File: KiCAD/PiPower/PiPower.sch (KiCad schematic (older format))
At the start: 19 parts

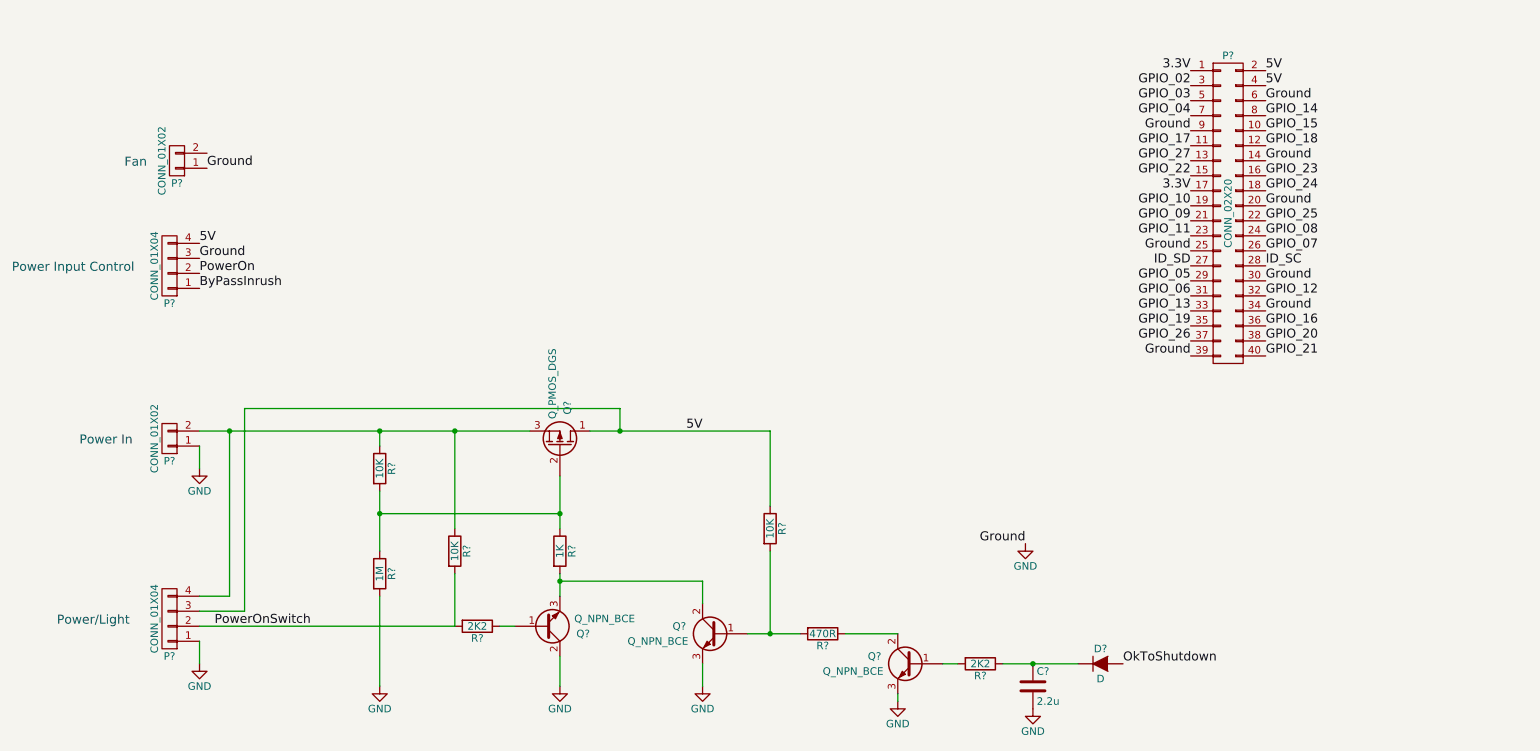
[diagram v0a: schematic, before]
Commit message: Raspberry Pi Power control board
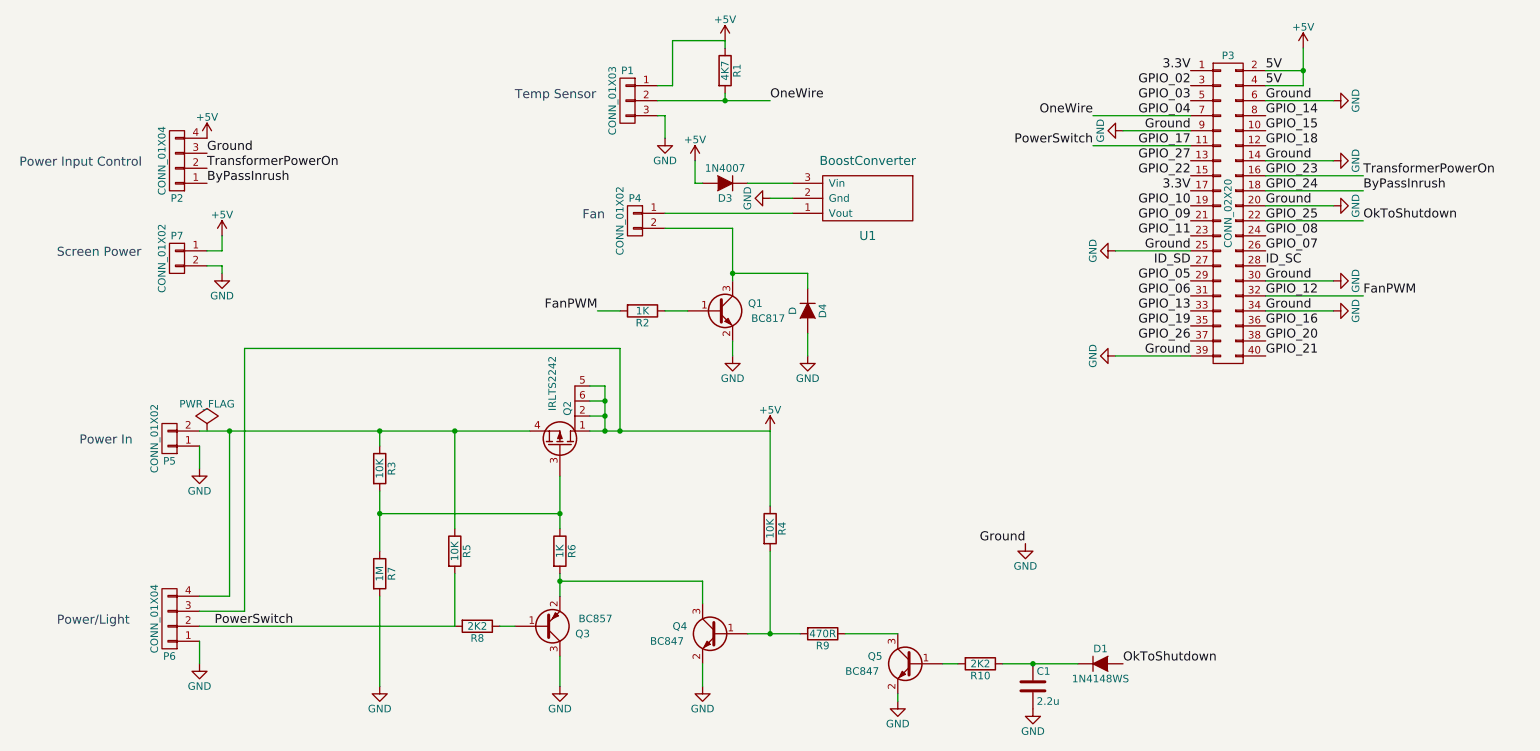
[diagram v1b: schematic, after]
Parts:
- removed P?: CONN_01X02, symbol CONN_01X02
- removed Q?: Q_PMOS_DGS, symbol Q_PMOS_DGS
- removed Q? (x3): Q_NPN_BCE, symbol Q_NPN_BCE
- added D3: 1N4007, Diodes_ThroughHole:Diode_DO-41_SOD81_Horizontal_RM10, symbol D
- added D4: D, Diodes_SMD:SOD-323, symbol D
- added P1: CONN_01X03, PinHead1-4:ThreePinSmall, symbol CONN_01X03
- added P4: CONN_01X02, PinHead1-4:TwoPinSmall, symbol CONN_01X02
- added P7: CONN_01X02, Pin_Headers:Pin_Header_Straight_1x02, symbol CONN_01X02
- added Q1: BC817, TO_SOT_Packages_SMD:SOT-23, symbol Q_NPN_BEC
- added Q2: IRLTS2242, symbol IRLTS2242
- added Q3: BC857, TO_SOT_Packages_SMD:SOT-23, symbol Q_PNP_BEC
- added Q4, Q5: BC847, TO_SOT_Packages_SMD:SOT-23, symbol Q_NPN_BEC
- added R1: 4K7, Resistors_SMD:R_0805, symbol R
- added R2: 1K, Resistors_SMD:R_0805, symbol R
- added U1: BoostConverter, BoostConverter:BoostConverter, symbol BoostConverter
- C1: renamed from C?; footprint (none) -> Capacitors_SMD:C_0805
- D1: renamed from D?; value D -> 1N4148WS; footprint (none) -> Diodes_SMD:SOD-323
- P2, P6: renamed from P?; footprint (none) -> PinHead1-4:PINHeader1-4
- P3: renamed from P?; footprint (none) -> Pin_Headers:Pin_Header_Straight_2x20
- P5: renamed from P?; footprint (none) -> wcon:WCON-2PIN
- R10, R3, R4, R5, R6, R7, R8, R9: renamed from R?; footprint (none) -> Resistors_SMD:R_0805
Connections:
- net GPIO_24 is gone; now on net ByPassInrush: P3.18 (P18)
- net OkToShutdown is gone; now on net GPIO_25: D1.2 (A)
- net PowerOn is gone; now on net GPIO_23: P2.2 (P2)
- net PowerOnSwitch is gone; now on net GPIO_17: P6.2 (P2), R5.2, R8.2
- net GND: now also D4.2 (A), P1.3 (P3), P7.2 (P2), Q1.2 (E), Q3.3 (C), Q4.2 (E), Q5.2 (E), U1.2 (Gnd)
- net GPIO_04: now also P1.2 (P2), R1.2
- net at R3.2, R6.1, R7.1: now also Q2.3 (G)
- net at P5.2 (P2), P6.4 (P4), R3.1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: now also Q2.4 (S)
- net at R6.2: now also Q3.2 (E), Q4.3 (C)
- net at R8.1: now also Q3.1 (B)
- net at R4.2, R9.2: now also Q4.1 (B)
- net at R10.2: now also Q5.1 (B)
- net at R9.1: now also Q5.3 (C)
- net 5V renamed +5V
- net +5V: now also D3.2 (A), P1.1 (P1), P7.1 (P1), Q2.1 (D), Q2.2 (D), Q2.5 (D), Q2.6 (D), R1.1
- net GPIO_12 renamed FanPWM
- net FanPWM: now also R2.2
- new net: Q1.1 (B), R2.1
- new net: D4.1 (K), P4.2 (P2), Q1.3 (C)
- new net: P4.1 (P1), U1.1 (Vout)
- new net: D3.1 (K), U1.3 (Vin)
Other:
- note added: "Fan"
- note added: "Screen Power"
- note added: "Temp Sensor\n"
- note removed: "Fan\n"
- moved on the sheet: P2
